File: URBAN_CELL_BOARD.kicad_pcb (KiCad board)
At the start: 2 copper layers, 162 x 181.6 mm, 18 parts, among them J1 Conn_02x09_Odd_Even, J2 Conn_01x02_Female, J3 Conn_01x02_Female

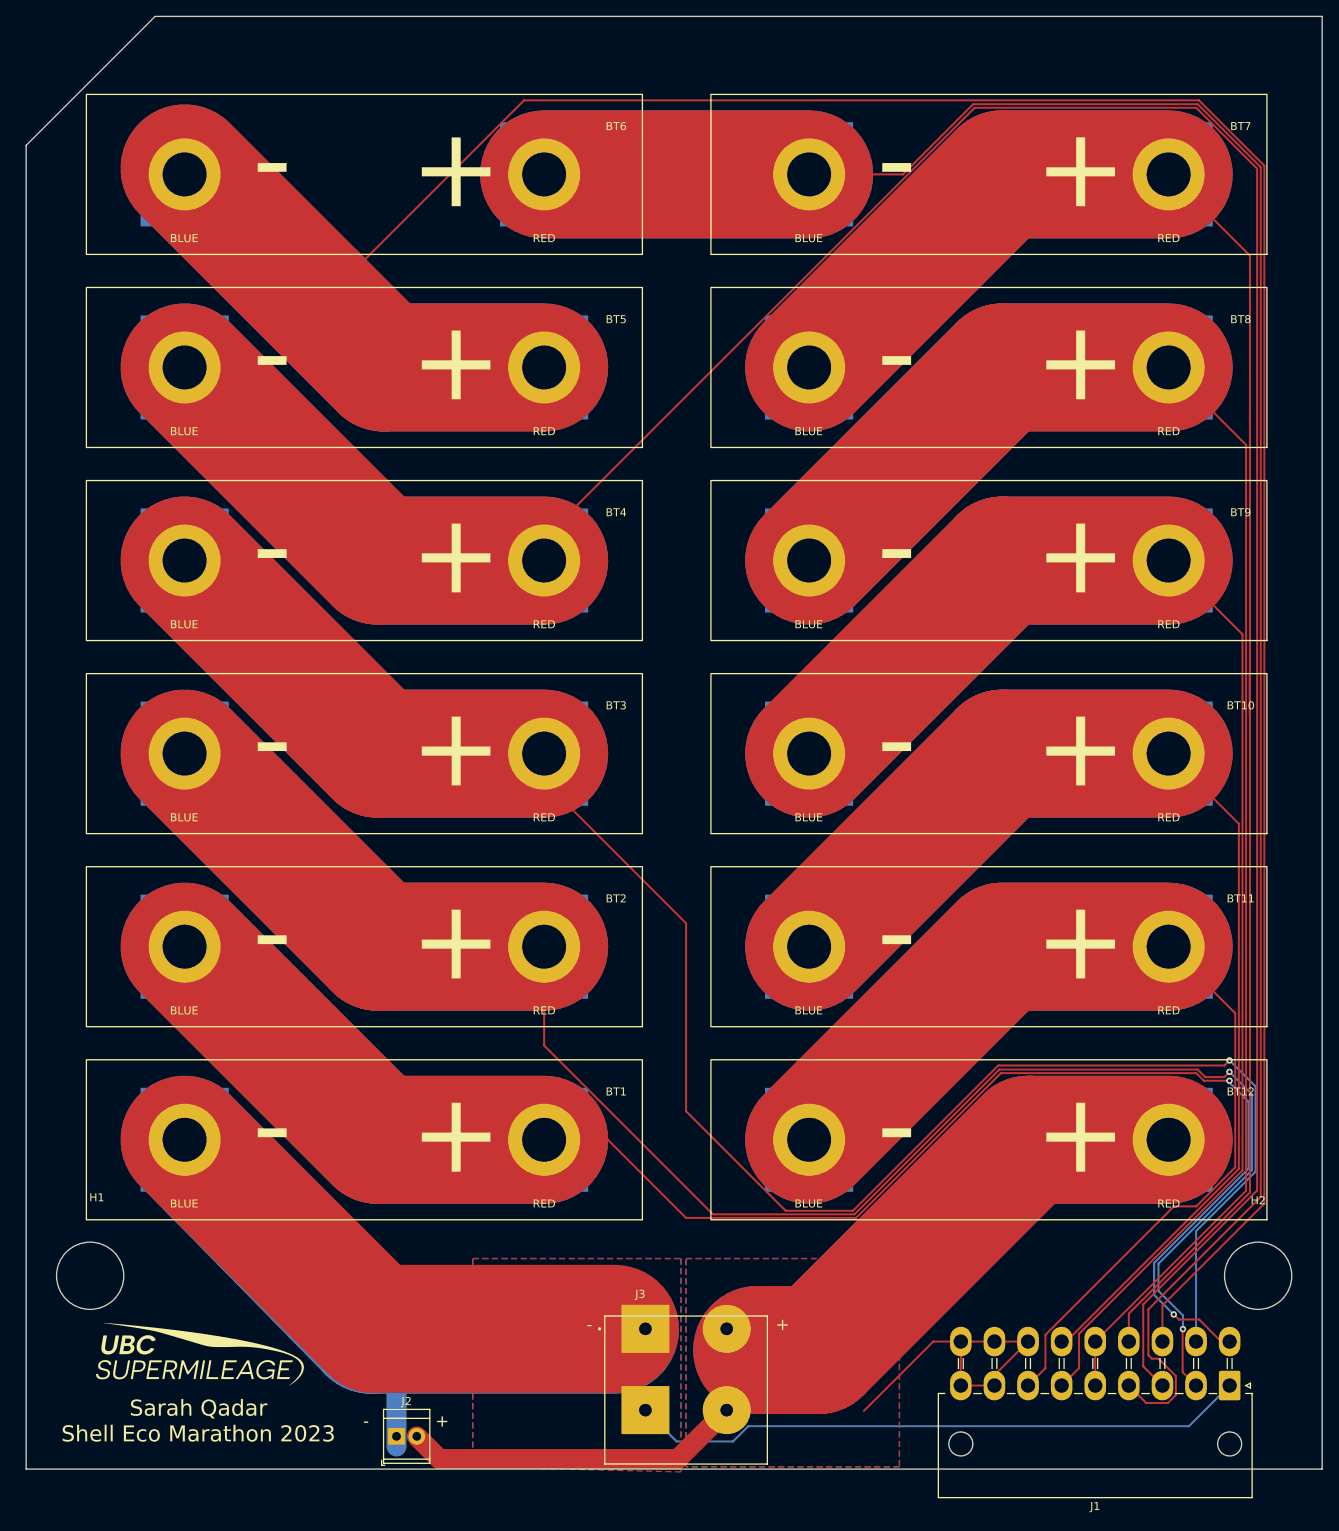
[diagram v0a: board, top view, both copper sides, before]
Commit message: fixes some cell positions
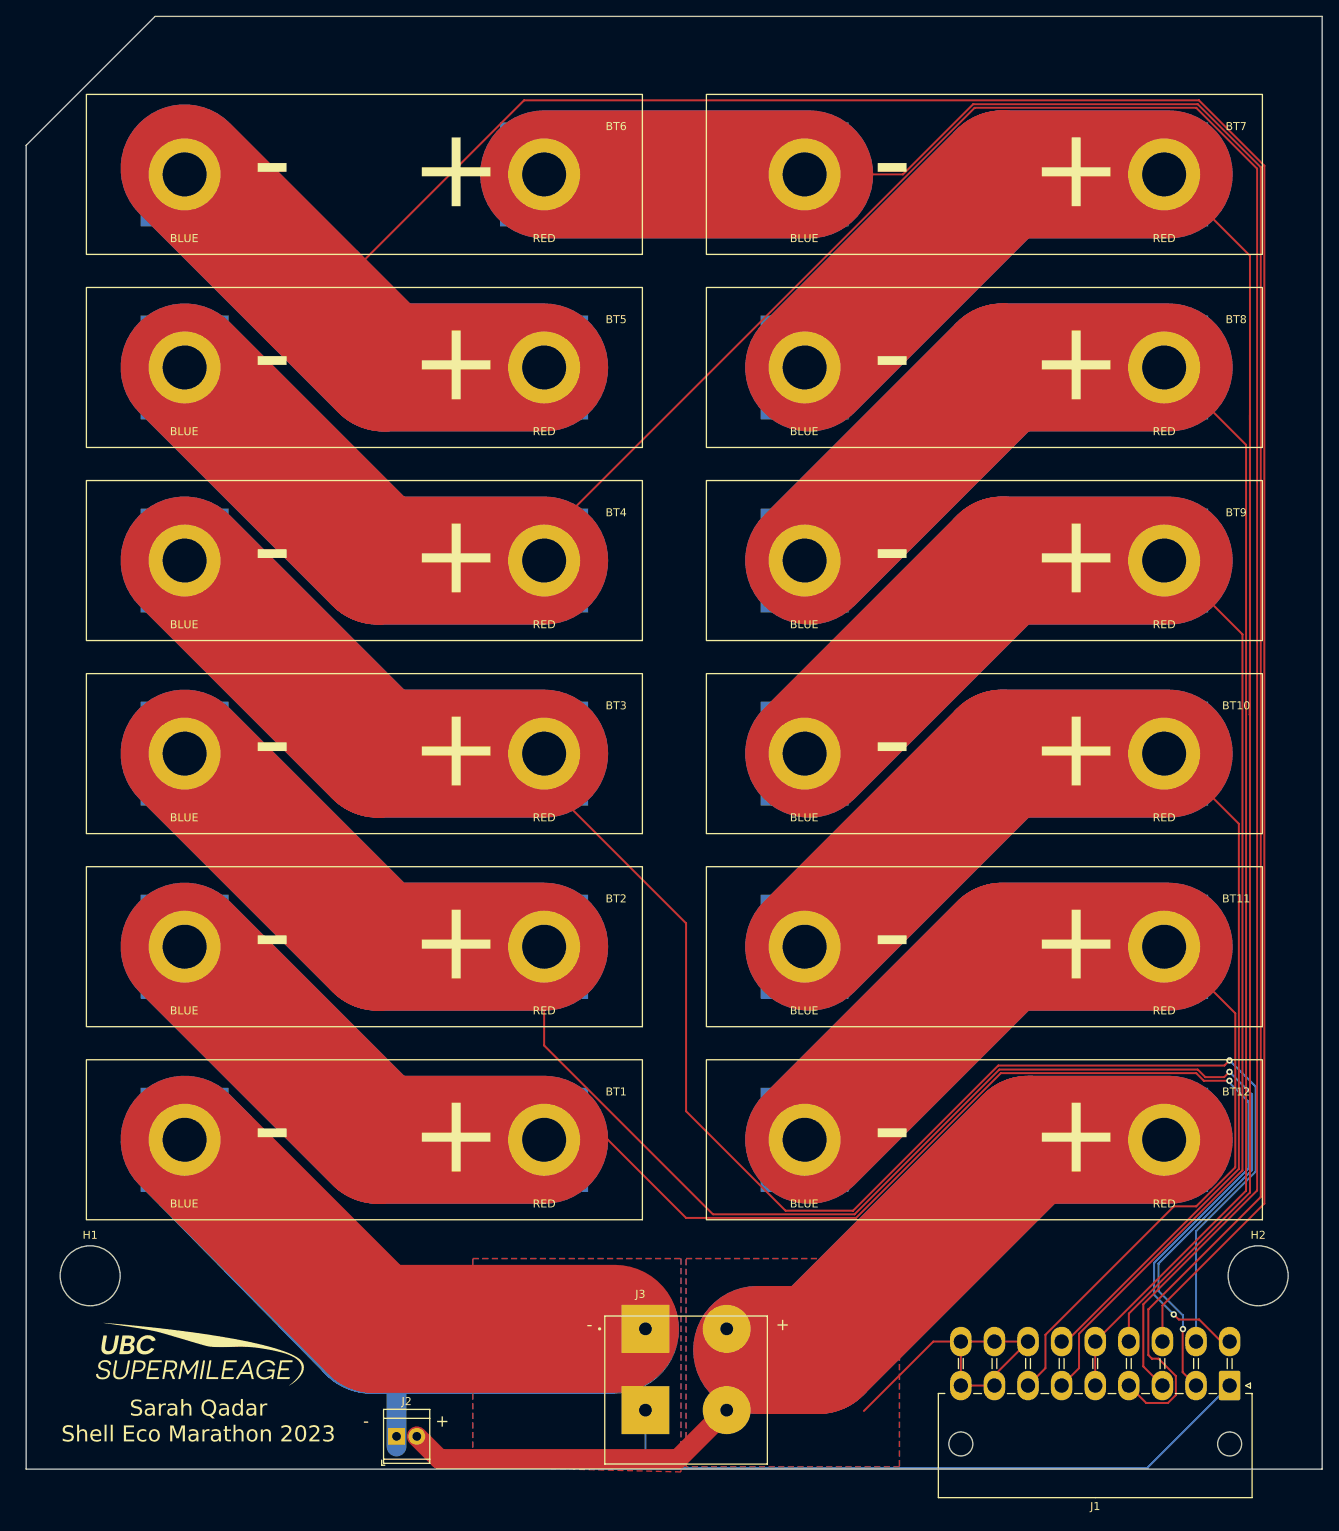
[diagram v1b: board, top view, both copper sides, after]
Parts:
- moved BT10 0.57 mm to (226.1, 192.2)
- moved BT11 0.57 mm to (226.1, 216.3)
- moved BT12 0.57 mm to (226.1, 240.4)
- moved BT7 0.57 mm to (226.1, 119.8)
- moved BT8 0.57 mm to (226.1, 143.9)
- moved BT9 0.57 mm to (226.1, 168.0)
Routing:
- net GND: track 220.8 -> 226.5 mm
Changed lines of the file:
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@@
   )
   (footprint "Battery:Energus Li1x4pVTC6T" (layer "F.Cu")
-    (at 226.695 119.75 180)
+    (at 226.129 119.75 180)
     (property "Sheetfile" "File: URBAN_CELL_BOARD.kicad_sch")
     (property "Sheetname" "")
@@
   )
   (footprint "Battery:Energus Li1x4pVTC6T" (layer "F.Cu")
-    (at 226.695 168.018 180)
+    (at 226.129 168.018 180)
     (property "Sheetfile" "File: URBAN_CELL_BOARD.kicad_sch")
     (property "Sheetname" "")
@@
   )
   (footprint "Battery:Energus Li1x4pVTC6T" (layer "F.Cu")
-    (at 226.695 192.153 180)
+    (at 226.129 192.153 180)
     (property "Sheetfile" "File: URBAN_CELL_BOARD.kicad_sch")
     (property "Sheetname" "")
@@
   )
   (footprint "Battery:Energus Li1x4pVTC6T" (layer "F.Cu")
-    (at 226.695 216.287 180)
+    (at 226.129 216.287 180)
     (property "Sheetfile" "File: URBAN_CELL_BOARD.kicad_sch")
     (property "Sheetname" "")
@@
     (property "Sheetname" "")
     (attr exclude_from_pos_files)
-    (fp_text reference "H2" (at 0 -9.4) (layer "F.SilkS")
-      (effects (font (size 1 1) (thickness 0.15)))
-    )
-    (fp_text value "MountingHole" (at 0 9.4) (layer "F.Fab")
+    (fp_text reference "H2" (at 0 -5.08) (layer "F.SilkS")
+      (effects (font (size 1 1) (thickness 0.15)))
+    )
+    (fp_text value "MountingHole" (at 0 5.08) (layer "F.Fab")
       (effects (font (size 1 1) (thickness 0.15)))
     )
@@
       (effects (font (size 1 1) (thickness 0.15)))
     )
-    (fp_circle (center 0 0) (end 8.4 0) (layer "Cmts.User") (width 0.15) (fill none))
-    (fp_circle (center 0 0) (end 8.65 0) (layer "F.CrtYd") (width 0.05) (fill none))
-    (pad "" np_thru_hole circle (at 0 0) (size 8.4 8.4) (drill 8.4) (layers *.Cu *.Mask))
+    (fp_circle (center 0 0) (end 4 0) (layer "Cmts.User") (width 0.15) (fill none))
+    (fp_circle (center 0 0) (end 4 0) (layer "F.CrtYd") (width 0.05) (fill none))
+    (pad "" np_thru_hole circle (at 0 0) (size 7.5 7.5) (drill 7.5) (layers F&B.Cu *.Mask))
   )
   (footprint "Battery:Energus Li1x4pVTC6T" (layer "F.Cu")
@@
   )
   (footprint "Battery:Energus Li1x4pVTC6T" (layer "F.Cu")
-    (at 226.695 240.421 180)
+    (at 226.129 240.421 180)
     (property "Sheetfile" "File: URBAN_CELL_BOARD.kicad_sch")
     (property "Sheetname" "")
@@
     (property "Sheetname" "")
     (attr exclude_from_pos_files)
-    (fp_text reference "H1" (at 0.831 -9.771) (layer "F.SilkS")
-      (effects (font (size 1 1) (thickness 0.15)))
-    )
-    (fp_text value "MountingHole" (at 0 9.4) (layer "F.Fab")
+    (fp_text reference "H1" (at 0 -5.08) (layer "F.SilkS")
+      (effects (font (size 1 1) (thickness 0.15)))
+    )
+    (fp_text value "MountingHole" (at 0 5.08) (layer "F.Fab")
       (effects (font (size 1 1) (thickness 0.15)))
     )
@@
       (effects (font (size 1 1) (thickness 0.15)))
     )
-    (fp_circle (center 0 0) (end 8.4 0) (layer "Cmts.User") (width 0.15) (fill none))
-    (fp_circle (center 0 0) (end 8.65 0) (layer "F.CrtYd") (width 0.05) (fill none))
-    (pad "" np_thru_hole circle (at 0 0) (size 8.4 8.4) (drill 8.4) (layers *.Cu *.Mask))
+    (fp_circle (center 0 0) (end 4 0) (layer "Cmts.User") (width 0.15) (fill none))
+    (fp_circle (center 0 0) (end 4 0) (layer "F.CrtYd") (width 0.05) (fill none))
+    (pad "" np_thru_hole circle (at 0 0) (size 7.5 7.5) (drill 7.5) (layers F&B.Cu *.Mask))
   )
   (footprint "Battery:Energus Li1x4pVTC6T" (layer "F.Cu")
@@
   )
   (footprint "Battery:Energus Li1x4pVTC6T" (layer "F.Cu")
-    (at 226.695 143.884 180)
+    (at 226.129 143.884 180)
     (property "Sheetfile" "File: URBAN_CELL_BOARD.kicad_sch")
     (property "Sheetname" "")
@@
   (segment (start 103.689 240.421) (end 127.3255 264.0575) (width 16) (layer "F.Cu") (net 2))
   (segment (start 130.175 267.335) (end 127 264.16) (width 0.25) (layer "B.Cu") (net 2))
+  (segment (start 161.29 279.29) (end 161.29 274.2175) (width 0.25) (layer "B.Cu") (net 2))
   (segment (start 103.689 240.421) (end 127 264.16) (width 16) (layer "B.Cu") (net 2))
-  (segment (start 172.239761 278.13) (end 165.2025 278.13) (width 0.25) (layer "B.Cu") (net 2))
+  (segment (start 163.459 281.459) (end 161.29 279.29) (width 0.25) (layer "B.Cu") (net 2))
   (segment (start 127 264.16) (end 157.48 264.16) (width 16) (layer "B.Cu") (net 2))
-  (segment (start 234.315 271.145) (end 229.235 276.225) (width 0.25) (layer "B.Cu") (net 2))
-  (segment (start 174.144761 276.225) (end 172.239761 278.13) (width 0.25) (layer "B.Cu") (net 2))
-  (segment (start 229.235 276.225) (end 174.144761 276.225) (width 0.25) (layer "B.Cu") (net 2))
+  (segment (start 224.001 281.459) (end 163.459 281.459) (width 0.25) (layer "B.Cu") (net 2))
   (segment (start 130.175 278.765) (end 130.175 267.335) (width 2.5) (layer "B.Cu") (net 2))
-  (segment (start 165.2025 278.13) (end 161.29 274.2175) (width 0.25) (layer "B.Cu") (net 2))
+  (segment (start 234.315 271.145) (end 224.001 281.459) (width 0.25) (layer "B.Cu") (net 2))
   (segment (start 148.629 216.287) (end 127.823 216.287) (width 16) (layer "F.Cu") (net 3))
   (segment (start 233.636342 232.595) (end 231.278724 232.595) (width 0.25) (layer "F.Cu") (net 3))

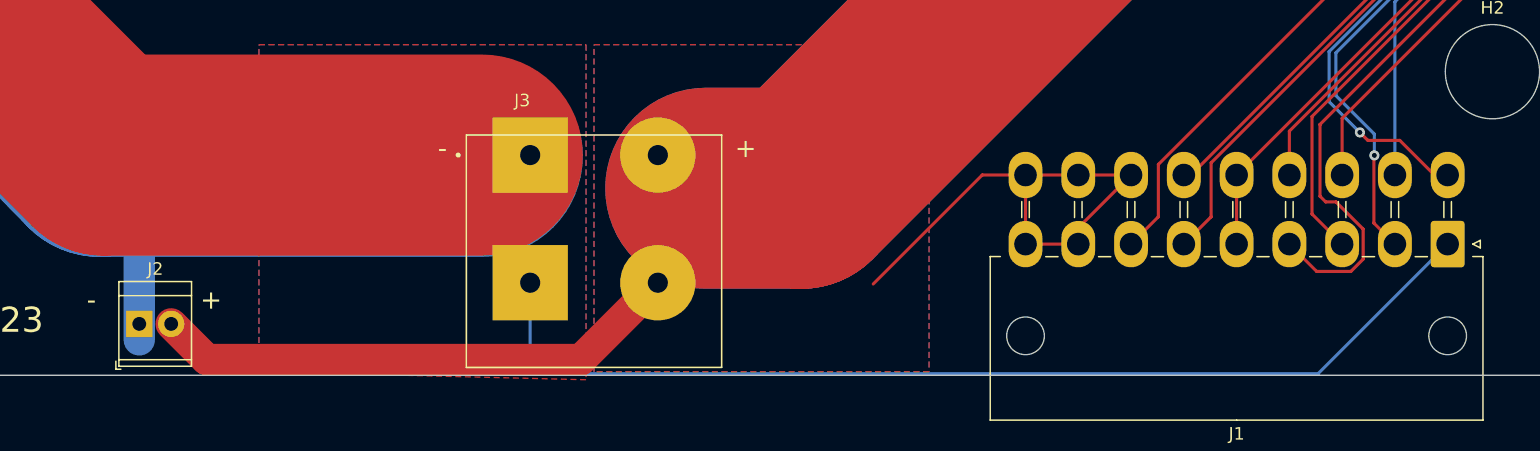
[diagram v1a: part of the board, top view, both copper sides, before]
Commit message: replaced charge terminal with two larger single position ones, fixed labelling
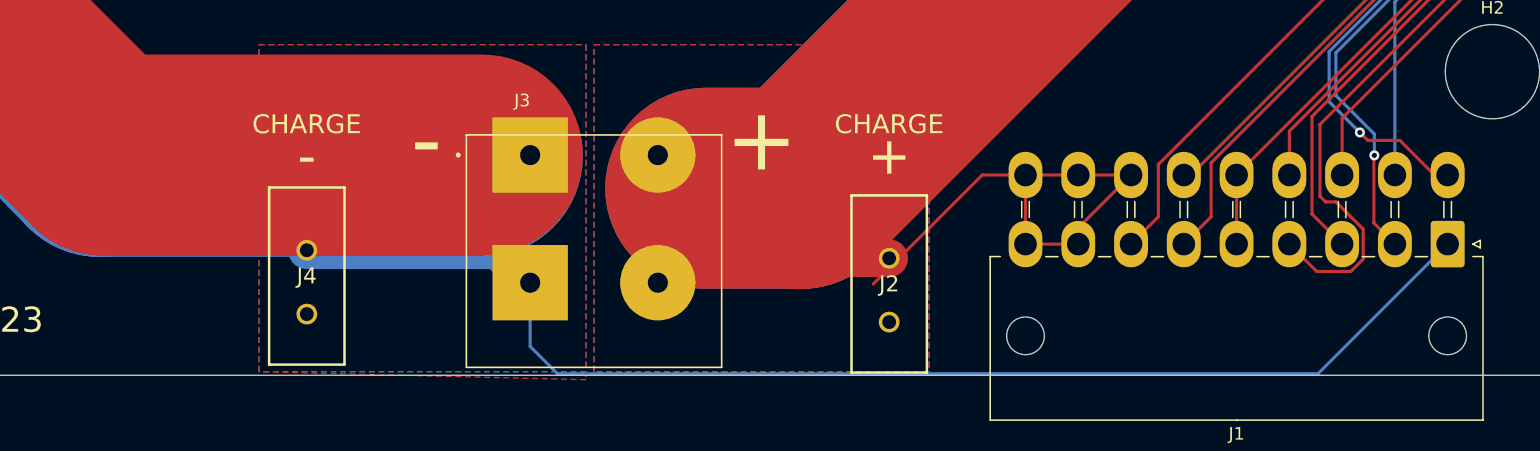
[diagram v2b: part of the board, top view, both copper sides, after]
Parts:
- added J4: Conn_01x01_Female, Phoenix_1889262:1889262, F.Cu at (143.5, 271.6)
- J2: value Conn_01x02_Female -> Conn_01x01_Female; footprint TerminalBlock_TE-Connectivity:TerminalBlock_TE_282834-2_1x02_P2.54mm_Horizontal -> Phoenix_1889262:1889262
- moved J2 59.9 mm to (189.9, 272.3)
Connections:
- J2 pad 1: GND -> +48V
- J2 pad 2: +48V -> (no net)
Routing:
- net +48V: track 208.1 -> 184.9 mm
- net GND: track 226.5 -> 233.9 mm
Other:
- board text added: "CHARGE"

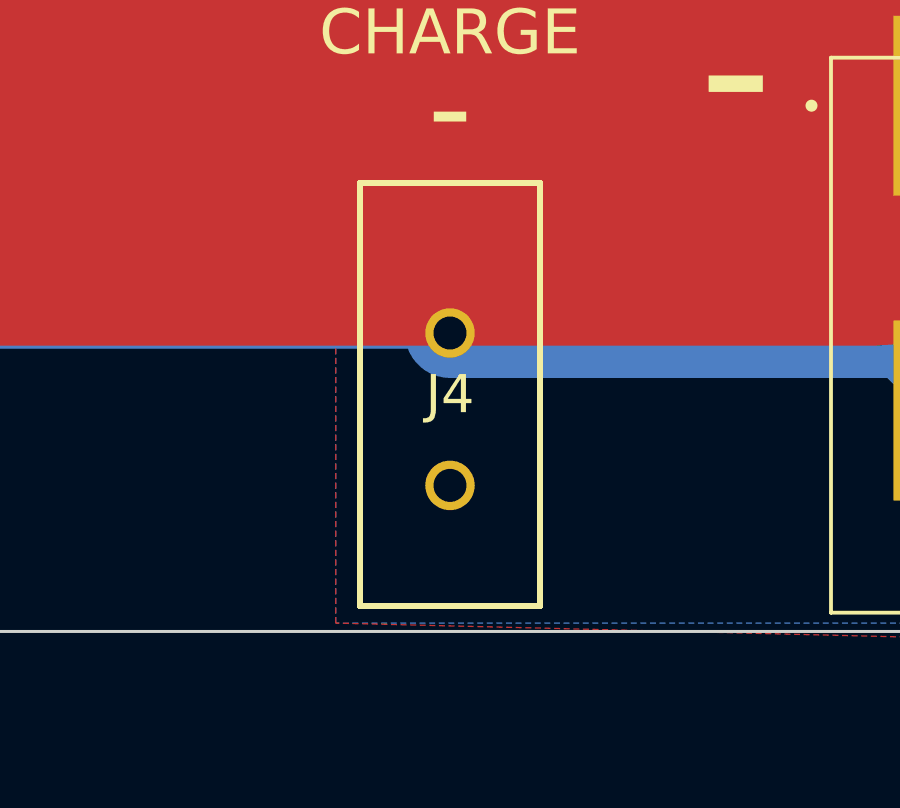
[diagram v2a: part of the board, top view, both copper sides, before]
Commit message: completed edits
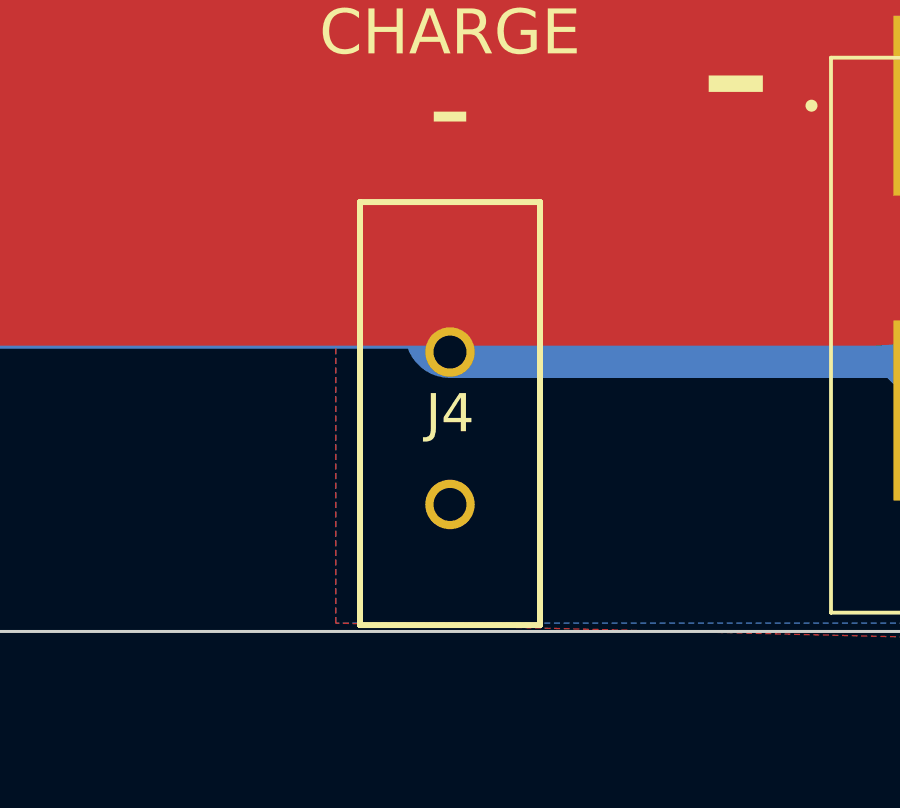
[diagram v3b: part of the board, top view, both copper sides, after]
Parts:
- moved J4 0.63 mm to (143.5, 272.3)
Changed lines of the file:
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@@
   )
   (footprint "Phoenix_1889262:1889262" (layer "F.Cu")
-    (at 143.51 271.635)
+    (at 143.51 272.27)
     (descr "1889262")
     (tags "Connector")
